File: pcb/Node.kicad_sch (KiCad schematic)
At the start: 0 parts

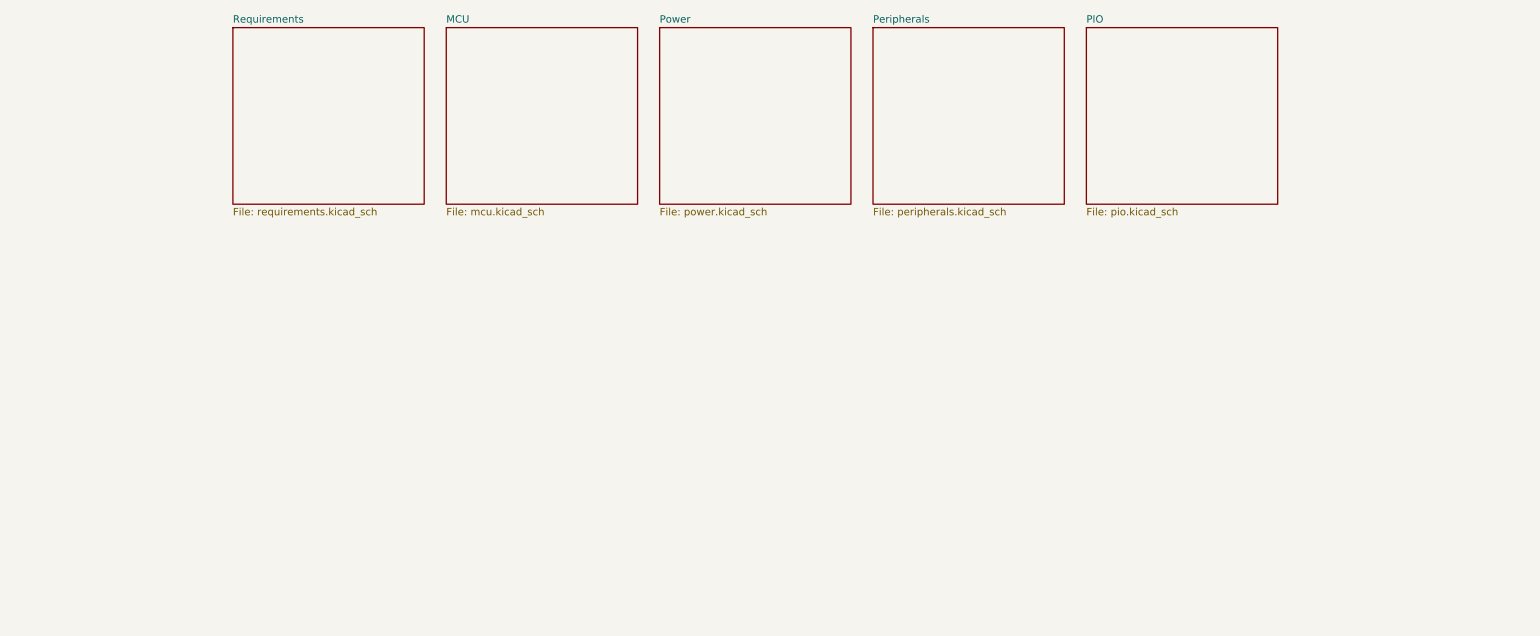
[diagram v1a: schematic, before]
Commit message: Major overhaul of IO
Added GPIO module
Added SPI interface
Added serial interface
Added power selection
Added power LEDs
Changed v3.3 LDO
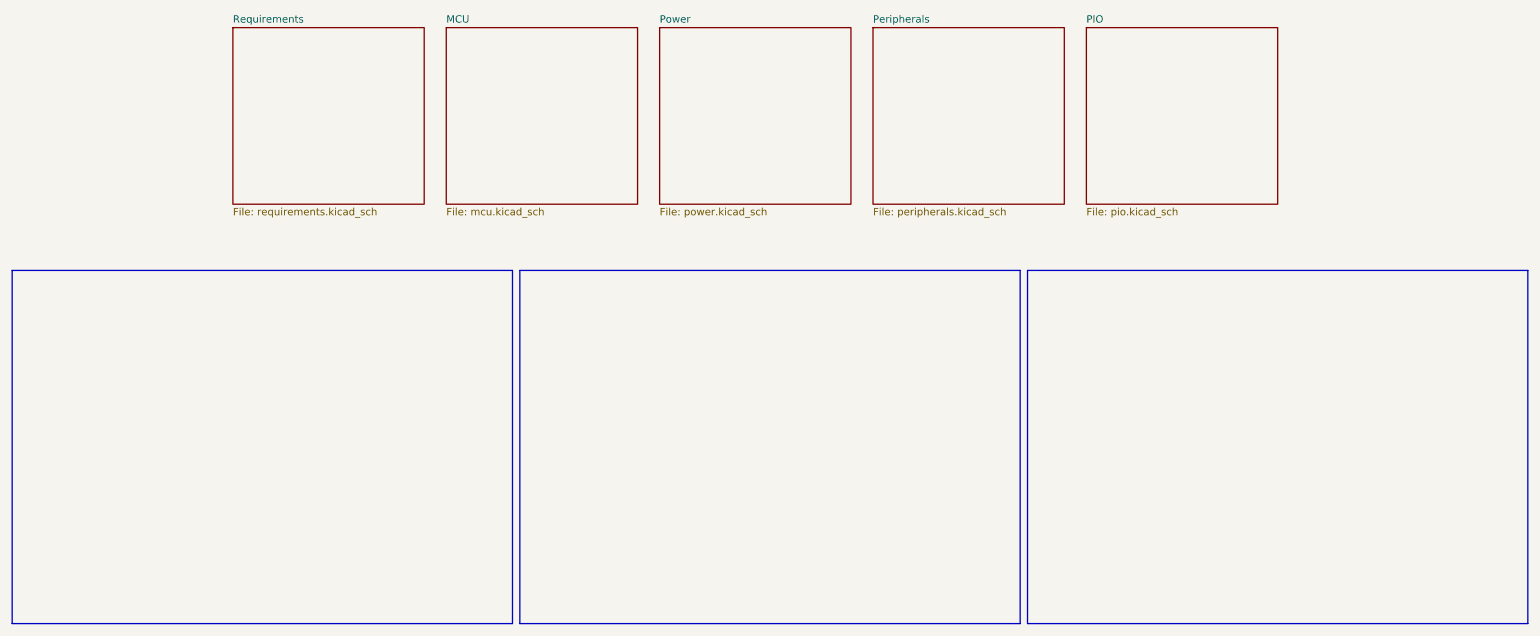
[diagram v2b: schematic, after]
